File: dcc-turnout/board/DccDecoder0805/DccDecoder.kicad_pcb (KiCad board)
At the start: 4 copper layers, 95 x 30 mm, 66 parts, among them J1 Conn_01x02, J10 Conn_01x01, J11 Conn_01x02, J12 Conn_01x01, J13 Conn_01x01, J14 Conn_01x02, J15 Conn_01x03, J16 Conn_01x02, J17 Conn_01x04, J2 Conn_01x02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

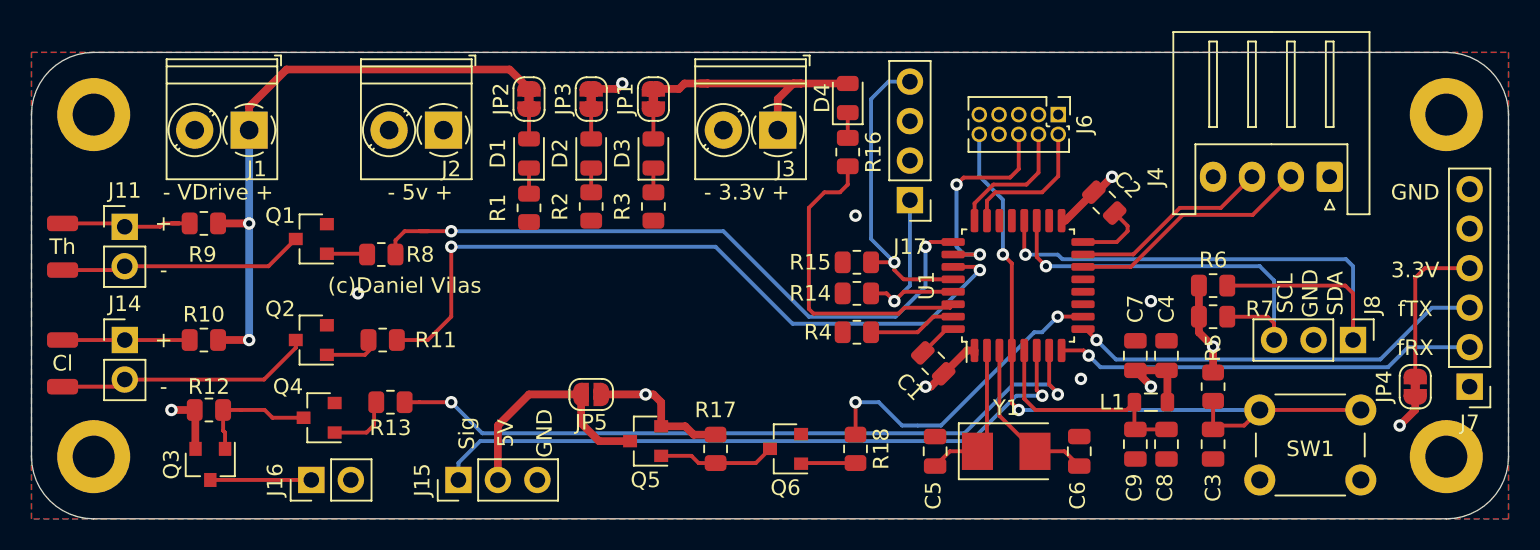
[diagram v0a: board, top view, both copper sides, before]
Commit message: update to Kicad 6
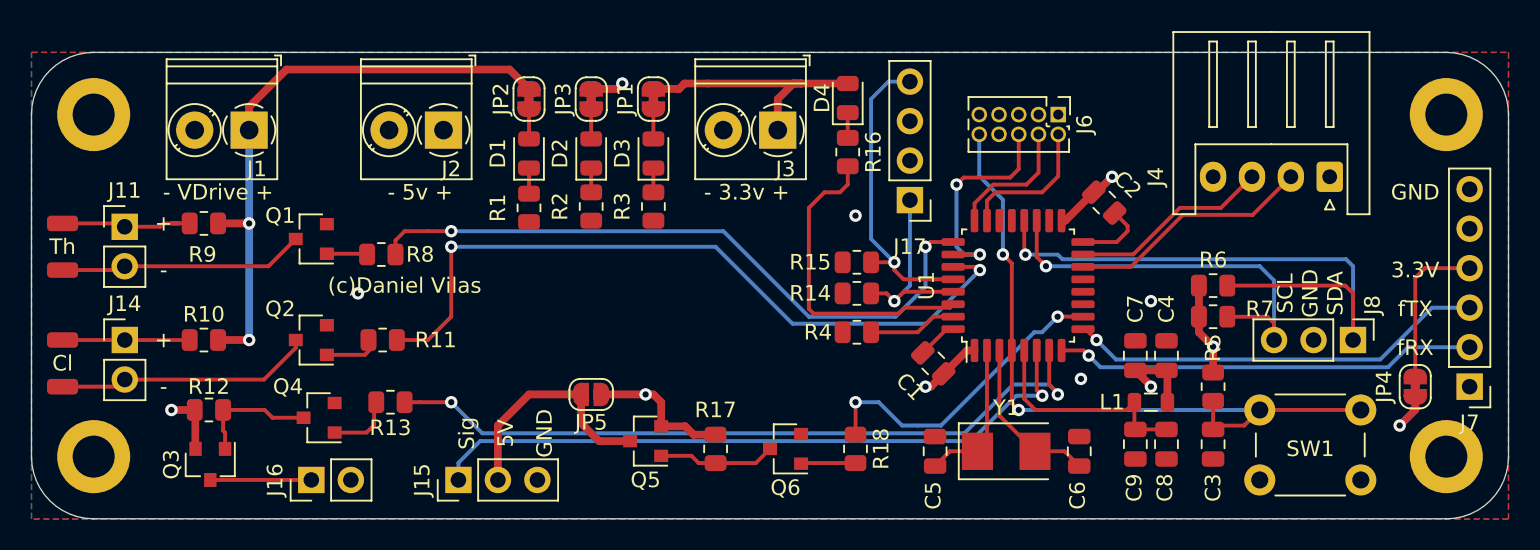
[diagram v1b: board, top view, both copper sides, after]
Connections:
- net /uC 030K6/NRST renamed /uC 030K6/RST
- net /uC 030K6/PF0 renamed /uC 030K6/OSC_IN
- net /uC 030K6/PF1 renamed /uC 030K6/OSC_OUT
- J6 pad 7: (no net) -> unconnected-(J6-Pad7)
- J6 pad 8: (no net) -> unconnected-(J6-Pad8)
- J7 pad 1: (no net) -> /F_DTR
- J7 pad 5: (no net) -> /F_CTS
- U1 pad 11: (no net) -> /uC 030K6/PA5
- U1 pad 12: (no net) -> /uC 030K6/PA6
- U1 pad 13: (no net) -> /uC 030K6/PA7
- U1 pad 18: (no net) -> /uC 030K6/PA8
- U1 pad 21: (no net) -> /uC 030K6/PA11
- U1 pad 22: (no net) -> /uC 030K6/PA12
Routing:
- net Net-(Q2-Pad1): track 4.14 -> 3.28 mm
- net +3V3: track 39.6 -> 38.9 mm
- net /ThrownLed: track 43.3 -> 42.8 mm
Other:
- net class Default removed
- net class Power removed

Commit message: Updates y mejoras
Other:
- board text added: "DCC Turnout Board V0.4.1"
- board text removed: "DCC Turnout Board V0.4.0"
